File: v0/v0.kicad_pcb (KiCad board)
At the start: 2 copper layers, 101.5 x 88.1 mm, 43 parts, among them CON1 SNES-CONN, M1 LY68L6400SLIT, U1 SN74LV165APWR, U2 SN74LV165APWR, U3 SN74LV165APWR, U4 SN74LVC8T245PWR, U5 PIC12F629-I/SN, U6 AMS1117-3.3, U7 SN74LVC8T245PWR, U8 Pair of 20-pin 1.27mm pitch v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

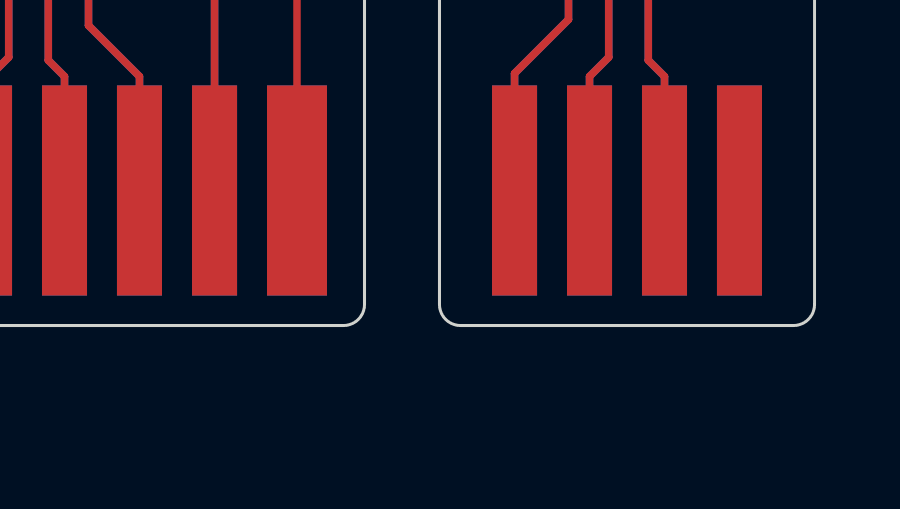
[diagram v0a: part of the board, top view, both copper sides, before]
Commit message: Add JLC properties; re-render front,back,pdf
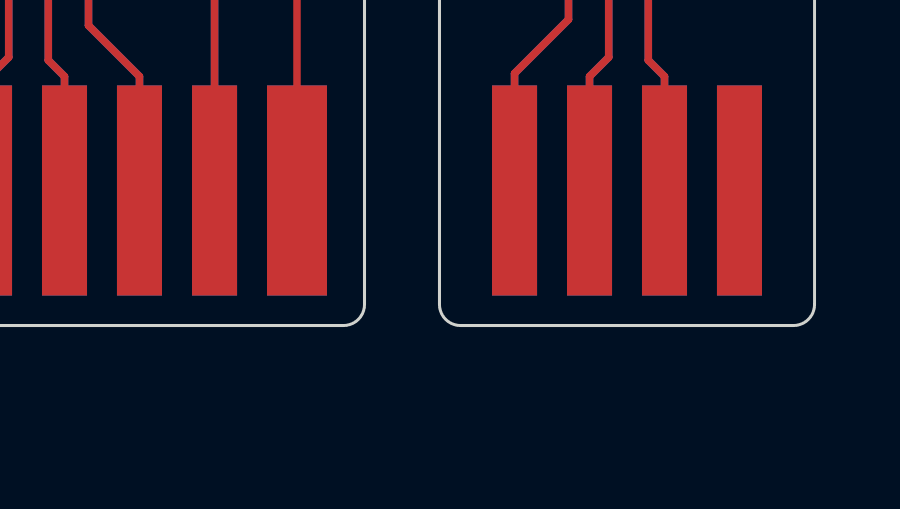
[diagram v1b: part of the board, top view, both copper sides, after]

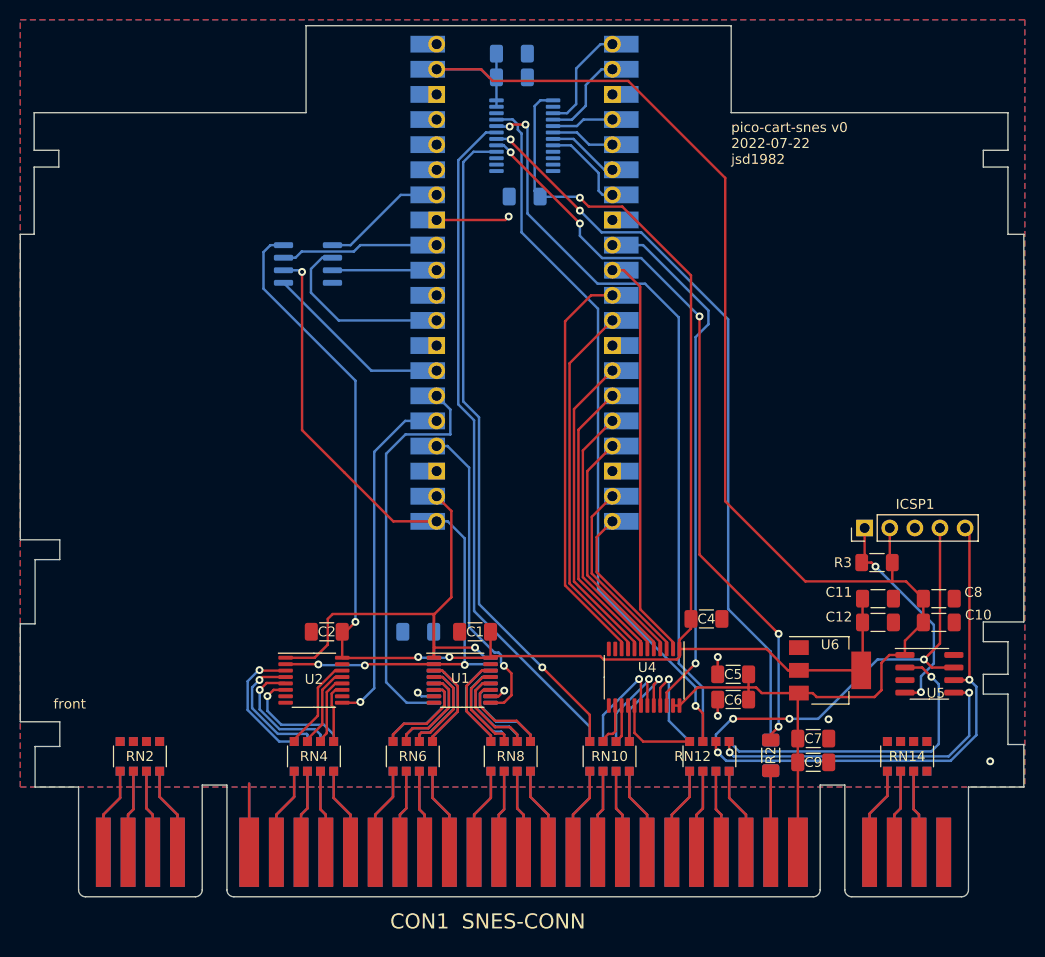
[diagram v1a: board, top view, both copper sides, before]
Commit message: Fix resistor array footprints and reroute; new layout of GPIO pins for PSRAM vs SNES address to be contiguous pin numbers
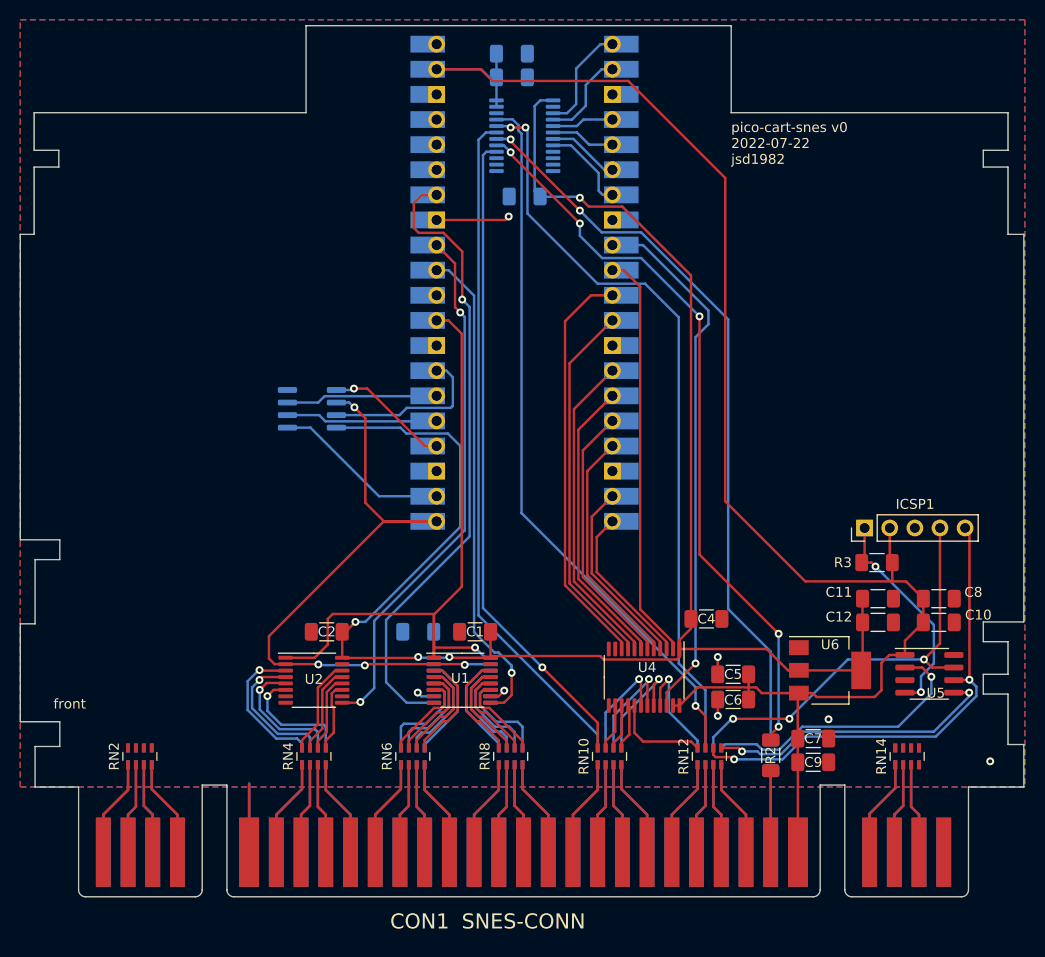
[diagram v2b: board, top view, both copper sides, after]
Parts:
- RN1, RN10, RN11, RN12, RN13, RN14, RN2, RN3, RN4, RN5, RN6, RN7, RN8, RN9: footprint Resistor_SMD:R_Array_Convex_4x1206 -> Resistor_SMD:R_Array_Concave_4x0603
- moved M1 14.7 mm to (115.8, 84.5), turned to 0 degrees
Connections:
- U8 pad 22: /U1~{LD} -> /PSRAM_~{CE}
- U8 pad 24: /U1QH -> /PSRAM_SIO0
- U8 pad 25: /U2QH -> /PSRAM_SIO1
- U8 pad 26: /U3QH -> /PSRAM_SIO2
- U8 pad 27: /PSRAM_SIO0 -> /PSRAM_SIO3
- U8 pad 29: /PSRAM_SIO1 -> /U1~{LD}
- U8 pad 31: /PSRAM_SIO2 -> /U1QH
- U8 pad 32: /PSRAM_SIO3 -> /U2QH
- U8 pad 34: /PSRAM_~{CE} -> /U3QH
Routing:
- net /U3QH: track 40.6 -> 64.1 mm, vias 0 -> 1
- net /U1~{LD}: track 46.1 -> 65.4 mm
- net /U2QH: track 35.4 -> 53.6 mm, vias 1 -> 2
- net /U1QH: track 31.7 -> 49.5 mm
- net +3.3V: track 183.1 -> 175.6 mm
- net /PSRAM_SIO0: track 19.2 -> 12.6 mm, vias 0 -> 1
- net /CLK_133MHZ: track 72.6 -> 67.0 mm
- net /PSRAM_~{CE}: track 12.6 -> 18.0 mm
- net /PSRAM_SIO2: track 10.5 -> 15.4 mm
- net /PSRAM_SIO1: track 18.9 -> 15.4 mm
- net /CIC_CLK: track 32.1 -> 28.7 mm
- net /CIC_OUT: track 51.8 -> 49.1 mm
- net /CIC_RST: track 32.3 -> 29.7 mm
- net /Y~{IRQ}: track 67.7 -> 66.3 mm
- net /YA12: track 13.3 -> 14.6 mm
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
